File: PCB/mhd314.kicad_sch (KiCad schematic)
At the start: 25 parts, among them Y1 25MHz

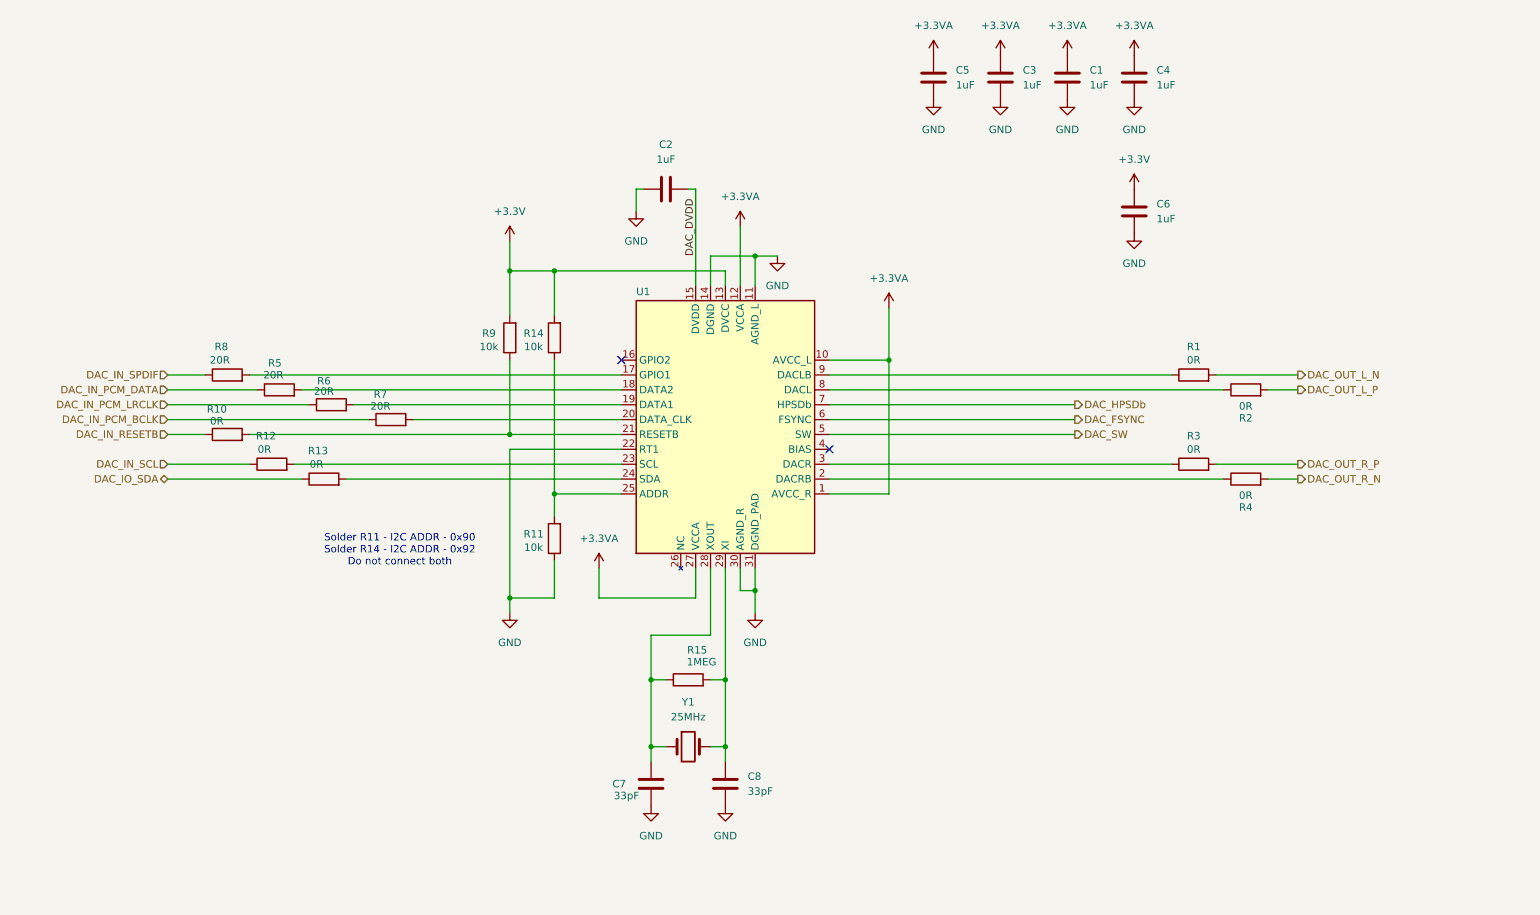
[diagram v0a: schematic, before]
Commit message: Finalized DAC and made it a module. Added Live 09 presentation
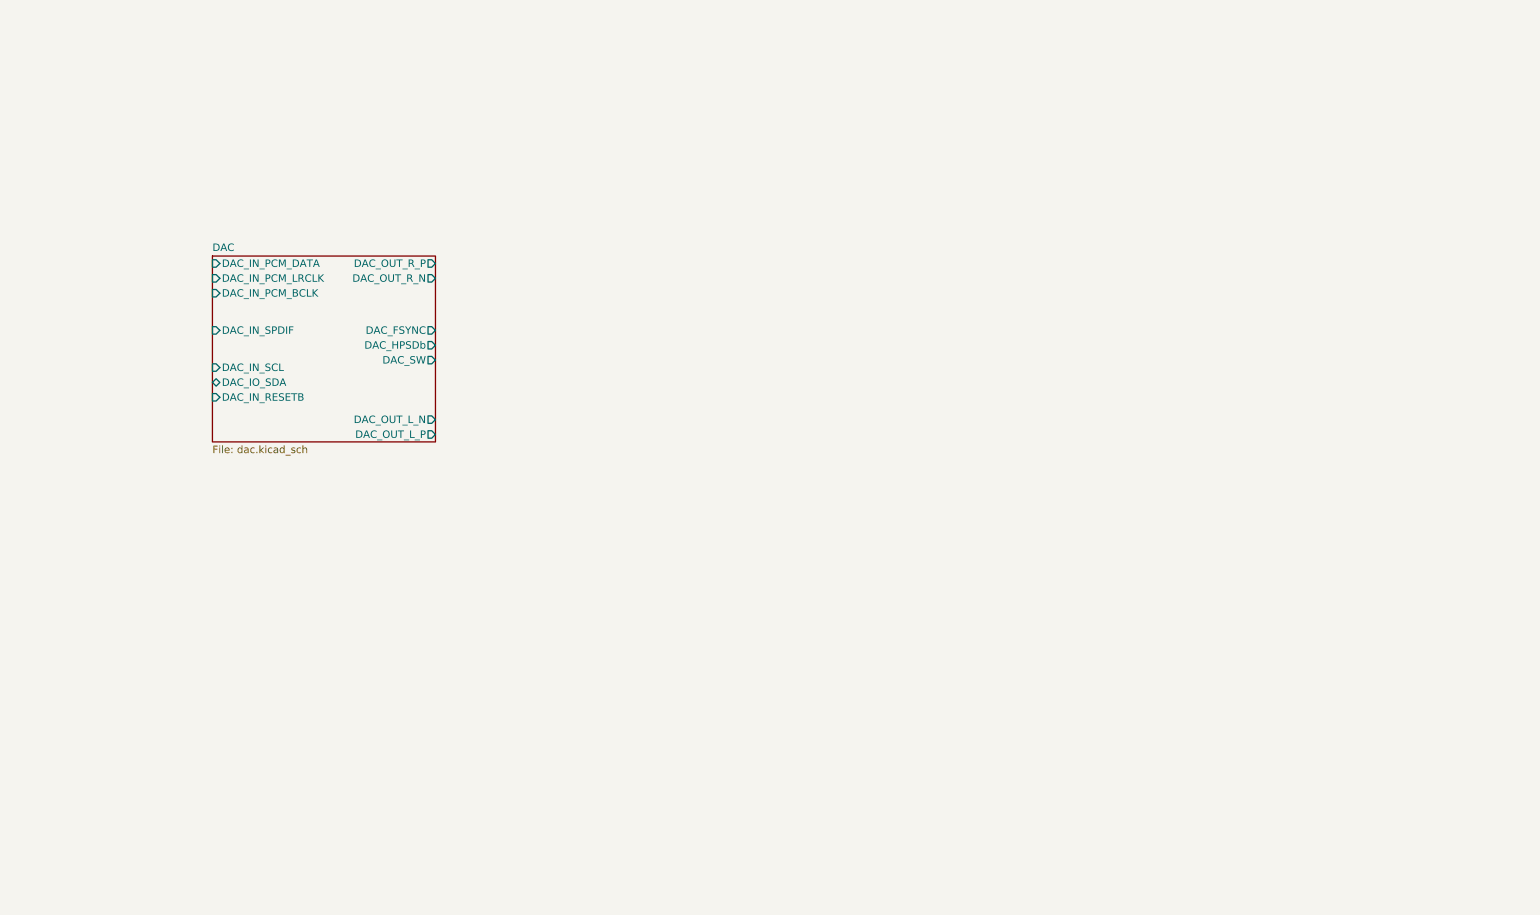
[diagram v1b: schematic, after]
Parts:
- removed C1, C2, C3, C4, C5, C6: 1uF, symbol Device:C
- removed C7, C8: 33pF, symbol Device:C
- removed R1, R10, R12, R13, R2, R3, R4: 0R, symbol Device:R
- removed R11, R14, R9: 10k, symbol Device:R
- removed R15: 1MEG, symbol Device:R
- removed R5, R6, R7, R8: 20R, symbol Device:R
- removed U1: ~, symbol mahaudio_kicad_lib:ES9038Q2M
- removed Y1: 25MHz, symbol Device:Crystal
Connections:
- no-connect marks 2 -> 0
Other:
- added sheet DAC (dac.kicad_sch)
- note removed: "Solder R11 - I2C ADDR - 0x90 Solder R14 - I2C ADDR - 0x92 Do not connect both"
- title: mahaudio HiFi DAC for RPi -> mahaudio HiFi DAC for RPi - Main Sheet

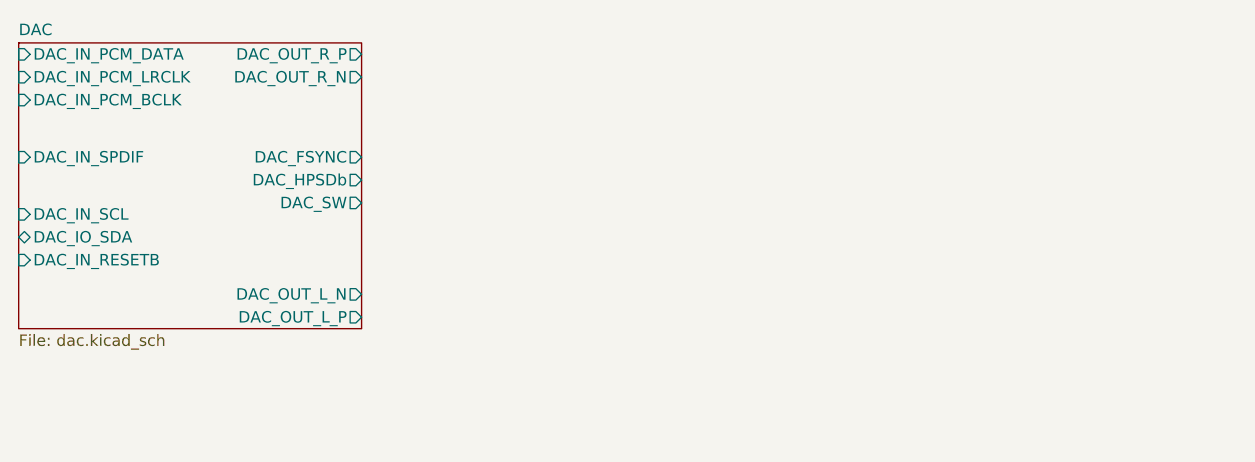
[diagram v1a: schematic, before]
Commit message: Added AMP stage circuits. Updated until Live 13
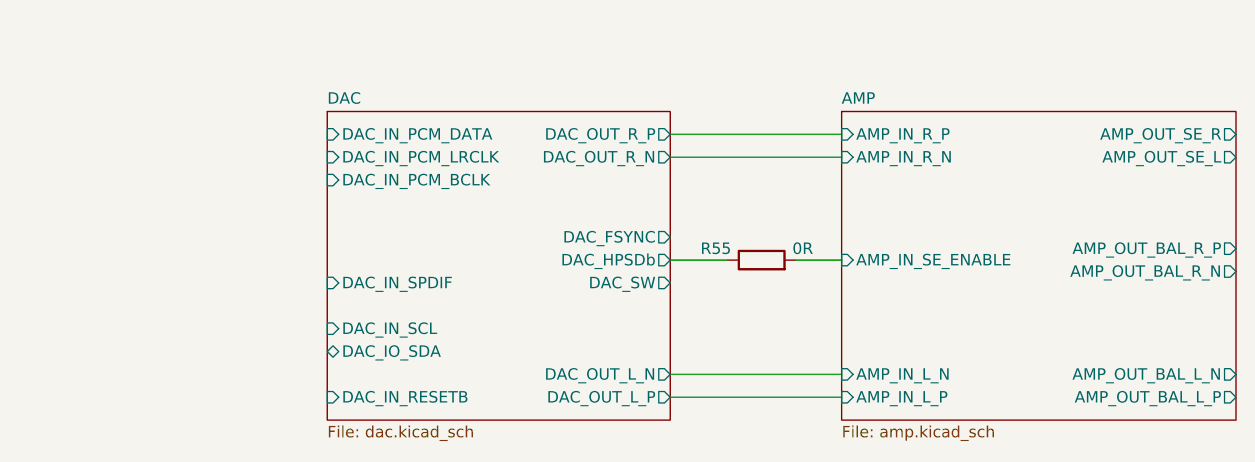
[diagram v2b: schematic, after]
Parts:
- added R55: 0R, Resistor_SMD:R_0402_1005Metric_Pad0.72x0.64mm_HandSolder, symbol Device:R
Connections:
- net DAC/DAC_HPSDb: now also R55.1
- new net AMP/AMP_IN_SE_ENABLE: R55.2
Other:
- added sheet AMP (amp.kicad_sch)

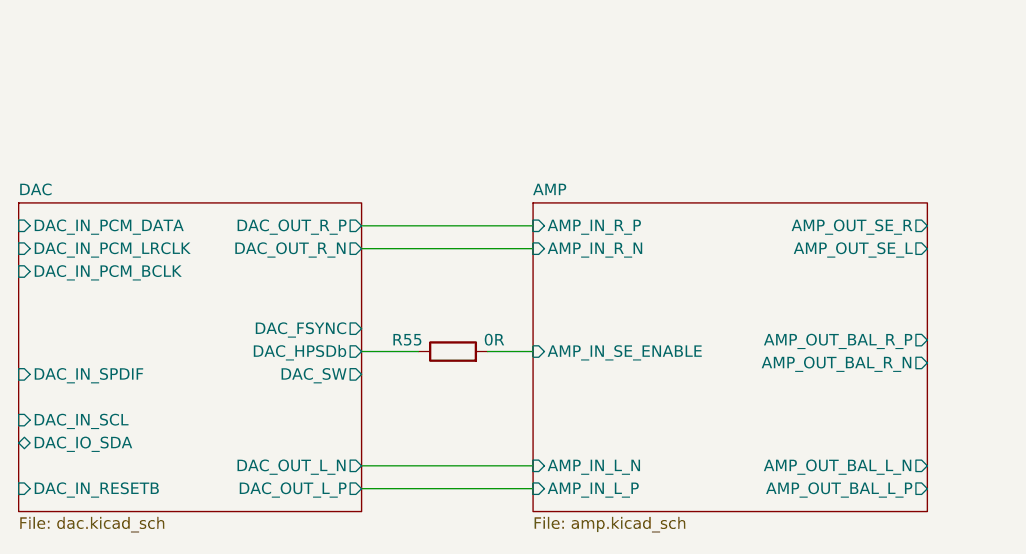
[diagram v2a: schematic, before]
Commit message: Added power supply and adjusted the AMP section to use only OPA1622 as output amp. In sync with Live 16
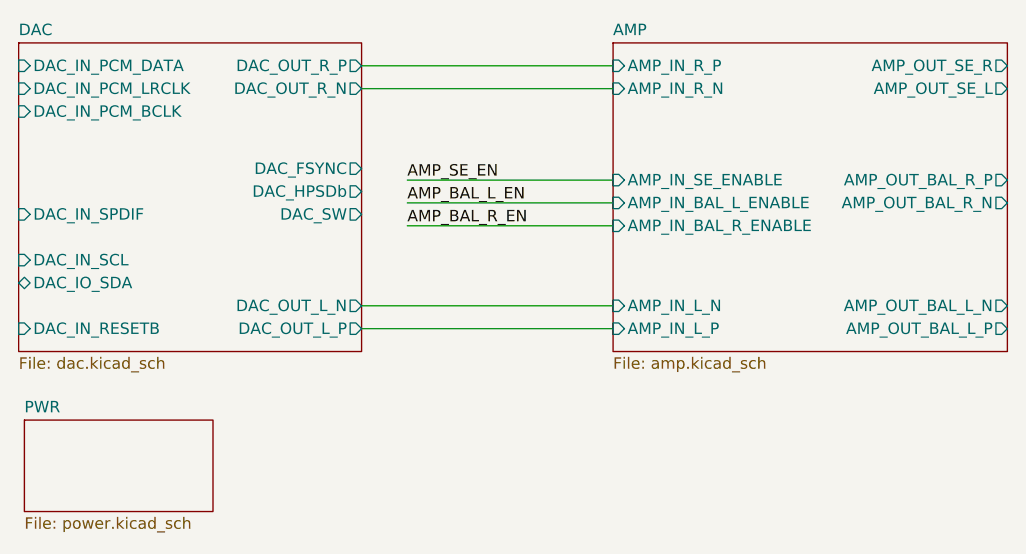
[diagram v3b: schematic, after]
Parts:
- removed R55: 0R, Resistor_SMD:R_0402_1005Metric_Pad0.72x0.64mm_HandSolder, symbol Device:R
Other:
- added sheet PWR (power.kicad_sch)
- sheet AMP ports: added AMP_IN_BAL_L_ENABLE, AMP_IN_BAL_R_ENABLE; removed none

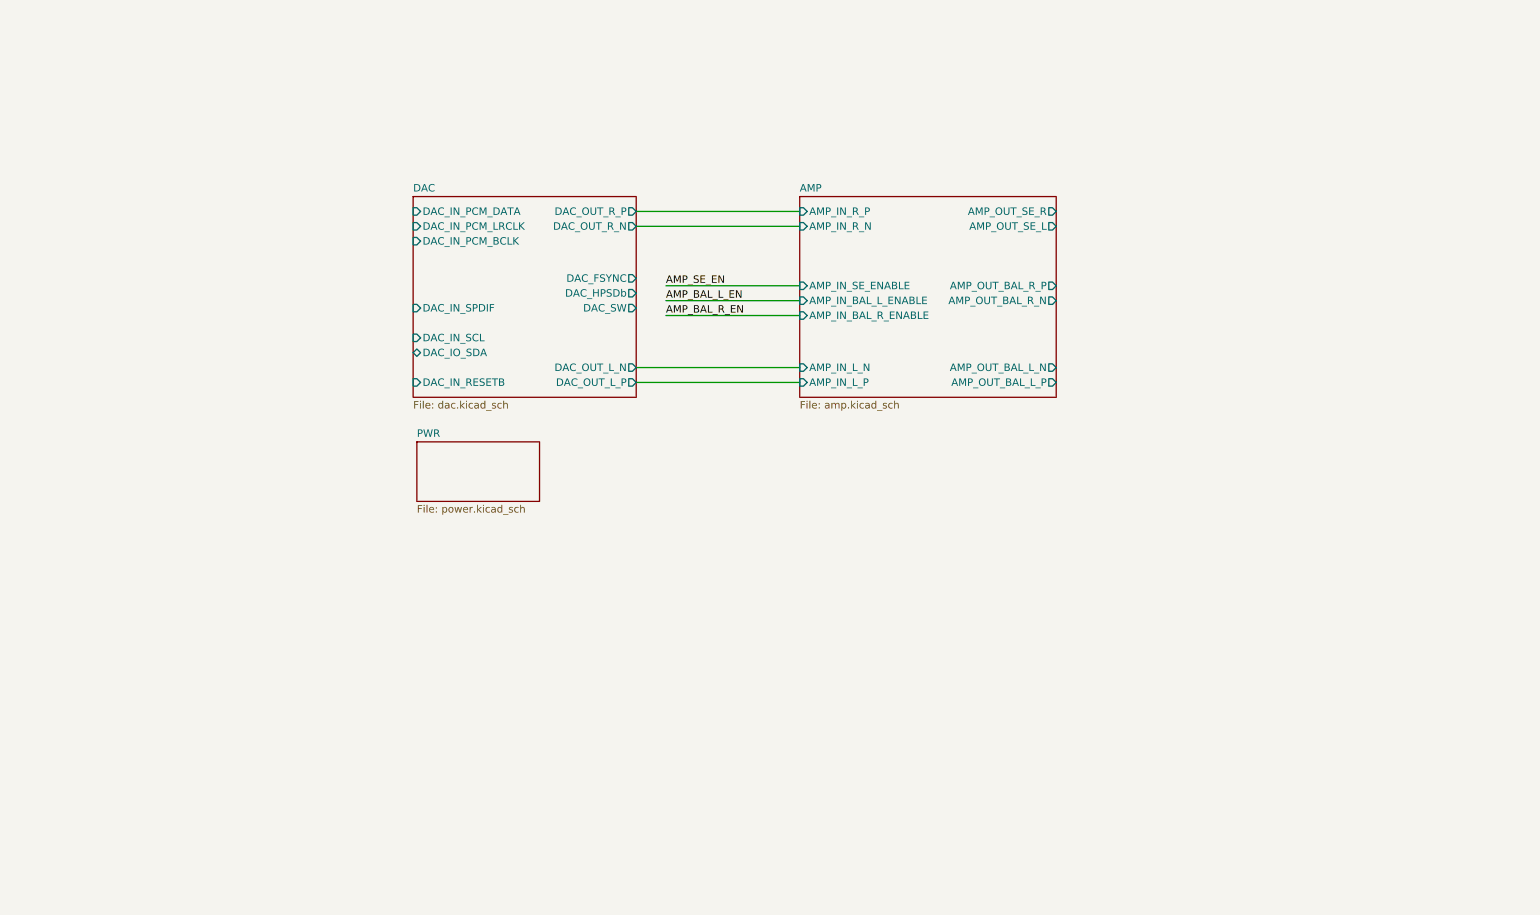
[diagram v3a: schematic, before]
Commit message: Added connectors
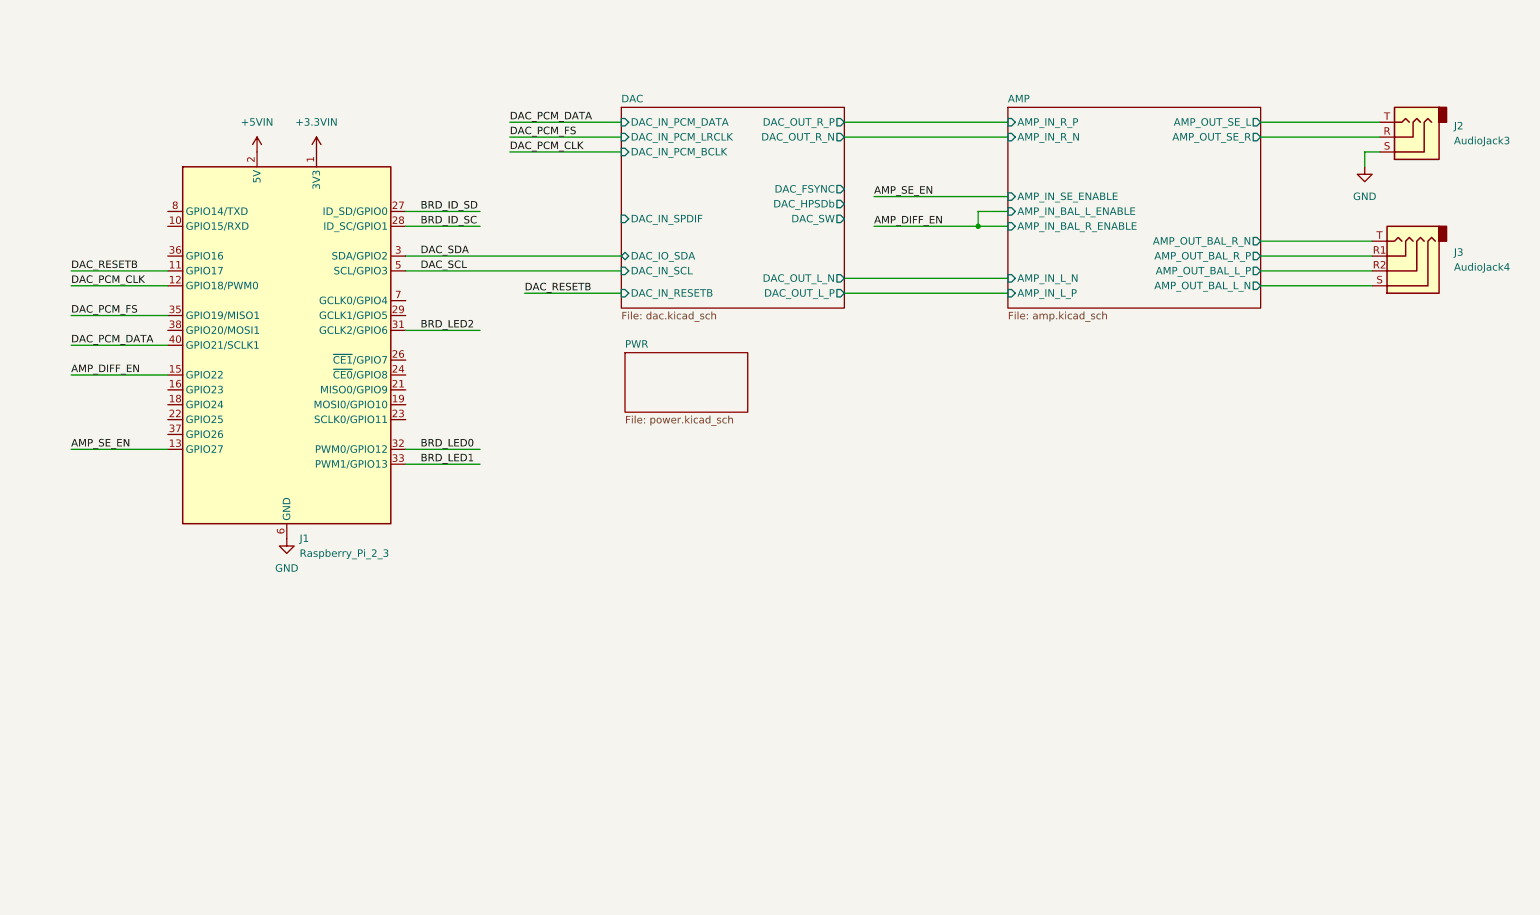
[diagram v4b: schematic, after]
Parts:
- added J1: Raspberry_Pi_2_3, symbol Connector:Raspberry_Pi_2_3
- added J2: AudioJack3, symbol Connector_Audio:AudioJack3
- added J3: AudioJack4, symbol Connector_Audio:AudioJack4
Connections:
- net AMP/AMP_OUT_BAL_L_N: now also J3.S
- net AMP/AMP_OUT_BAL_L_P: now also J3.R2
- net AMP/AMP_OUT_BAL_R_N: now also J3.T
- net AMP/AMP_OUT_BAL_R_P: now also J3.R1
- net AMP/AMP_OUT_SE_L: now also J2.T
- net AMP/AMP_OUT_SE_R: now also J2.R
- net AMP_SE_EN: now also J1.13 (GPIO27)
- new net +3.3VIN: J1.1 (3V3), J1.17 (3V3)
- new net +5VIN: J1.2 (5V), J1.4 (5V)
- new net AMP_DIFF_EN: J1.15 (GPIO22)
- new net BRD_ID_SC: J1.28 (ID_SC/GPIO1)
- new net BRD_ID_SD: J1.27 (ID_SD/GPIO0)
- new net BRD_LED0: J1.32 (PWM0/GPIO12)
- new net BRD_LED1: J1.33 (PWM1/GPIO13)
- new net BRD_LED2: J1.31 (GCLK2/GPIO6)
- new net DAC_PCM_CLK: J1.12 (GPIO18/PWM0)
- new net DAC_PCM_DATA: J1.40 (GPIO21/SCLK1)
- new net DAC_PCM_FS: J1.35 (GPIO19/MISO1)
- new net DAC_RESETB: J1.11 (GPIO17)
- new net DAC_SCL: J1.5 (SCL/GPIO3)
- new net DAC_SDA: J1.3 (SDA/GPIO2)
- new net GND: J1.14 (GND), J1.20 (GND), J1.25 (GND), J1.30 (GND), J1.34 (GND), J1.39 (GND), J1.6 (GND), J1.9 (GND), J2.S
